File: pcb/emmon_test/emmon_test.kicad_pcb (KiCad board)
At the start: 2 copper layers, 11 parts, among them J1 Conn_01x06_Female, J2 Conn_01x08_Female, J3 Conn_01x15_Female, J4 Conn_01x15_Female, J5 Conn_01x04_Female

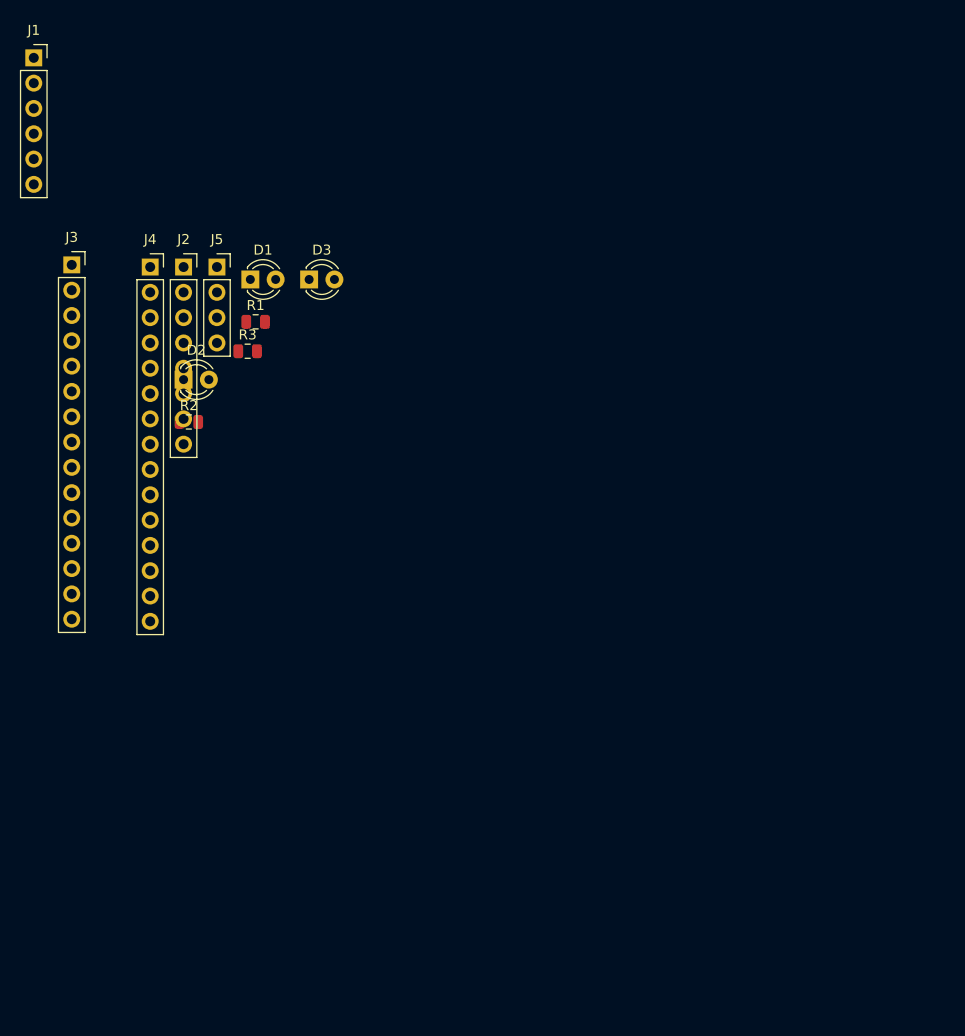
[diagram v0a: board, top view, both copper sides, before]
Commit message: se implementa oop en el codigo y se edita el pcb
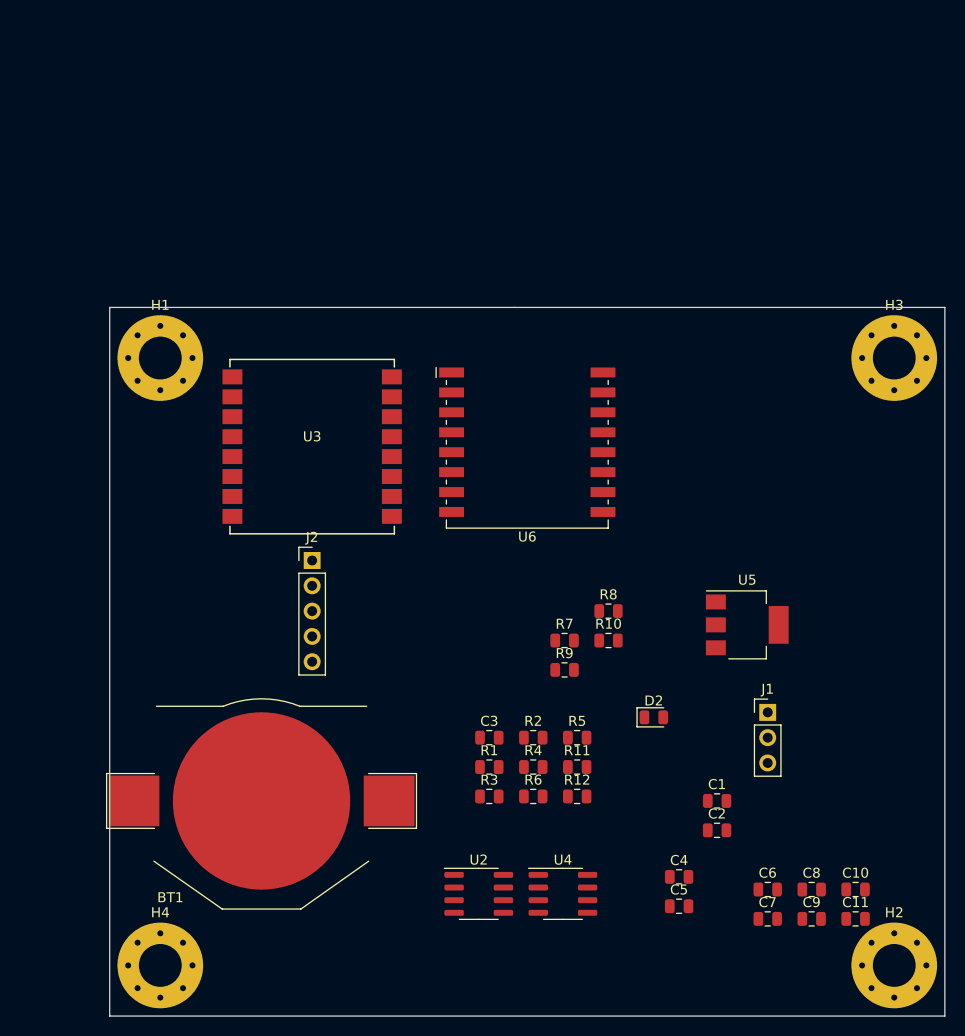
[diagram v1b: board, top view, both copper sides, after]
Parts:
- removed D1, D3: LED, LED_THT:LED_D3.0mm
- removed J3, J4: Conn_01x15_Female, Connector_PinSocket_2.54mm:PinSocket_1x15_P2.54mm_Vertical
- removed J5: Conn_01x04_Female, Connector_PinSocket_2.54mm:PinSocket_1x04_P2.54mm_Vertical
- added BT1: Battery_Cell, Battery:BatteryHolder_Keystone_3002_1x2032, F.Cu at (129.5, 105.4)
- added C1: 100n, Capacitor_SMD:C_0805_2012Metric, F.Cu at (175.3, 105.4)
- added C10: 10u, Capacitor_SMD:C_0805_2012Metric, F.Cu at (189.2, 114.3)
- added C11: 100n, Capacitor_SMD:C_0805_2012Metric, F.Cu at (189.2, 117.2)
- added C2: 47u, Capacitor_SMD:C_0805_2012Metric, F.Cu at (175.3, 108.4)
- added C3: 47p, Capacitor_SMD:C_0805_2012Metric, F.Cu at (152.4, 99.1)
- added C4: 10u, Capacitor_SMD:C_0805_2012Metric, F.Cu at (171.4, 113.0)
- added C5: 100n, Capacitor_SMD:C_0805_2012Metric, F.Cu at (171.4, 116.0)
- added C6: 10u, Capacitor_SMD:C_0805_2012Metric, F.Cu at (180.3, 114.3)
- added C7: 100n, Capacitor_SMD:C_0805_2012Metric, F.Cu at (180.3, 117.2)
- added C8: 10u, Capacitor_SMD:C_0805_2012Metric, F.Cu at (184.8, 114.3)
- added C9: 100n, Capacitor_SMD:C_0805_2012Metric, F.Cu at (184.8, 117.2)
- added H1: MountingHole_Pad, MountingHole:MountingHole_4.3mm_M4_Pad_Via, F.Cu at (119.4, 61.0)
- added H2: MountingHole_Pad, MountingHole:MountingHole_4.3mm_M4_Pad_Via, F.Cu at (193.0, 121.9)
- added H3: MountingHole_Pad, MountingHole:MountingHole_4.3mm_M4_Pad_Via, F.Cu at (193.0, 61.0)
- added H4: MountingHole_Pad, MountingHole:MountingHole_4.3mm_M4_Pad_Via, F.Cu at (119.4, 121.9)
- added R10: 12K, Resistor_SMD:R_0805_2012Metric, F.Cu at (164.4, 89.3)
- added R11: 12K, Resistor_SMD:R_0805_2012Metric, F.Cu at (161.2, 102.0)
- added R12: 12K, Resistor_SMD:R_0805_2012Metric, F.Cu at (161.2, 105.0)
- added R4: 12K, Resistor_SMD:R_0805_2012Metric, F.Cu at (156.8, 102.0)
- added R5: 12K, Resistor_SMD:R_0805_2012Metric, F.Cu at (161.2, 99.1)
- added R6: 12K, Resistor_SMD:R_0805_2012Metric, F.Cu at (156.8, 105.0)
- added R7: 12K, Resistor_SMD:R_0805_2012Metric, F.Cu at (159.9, 89.3)
- added R8: 12K, Resistor_SMD:R_0805_2012Metric, F.Cu at (164.4, 86.4)
- added R9: 12K, Resistor_SMD:R_0805_2012Metric, F.Cu at (159.9, 92.3)
- added U2: DS3231MZ, Package_SO:SOIC-8_3.9x4.9mm_P1.27mm, F.Cu at (151.3, 114.7)
- added U3: Ai-Thinker-Ra-01, RF_Module:Ai-Thinker-Ra-01-LoRa, F.Cu at (134.6, 69.8)
- added U4: AT24CS32-SSHM, Package_SO:SOIC-8_3.9x4.9mm_P1.27mm, F.Cu at (159.8, 114.7)
- added U5: AMS1117-3.3, Package_TO_SOT_SMD:SOT-223-3_TabPin2, F.Cu at (178.3, 87.7)
- added U6: ESP-07, RF_Module:ESP-07, F.Cu at (156.2, 67.3)
- D2: value LED -> LED_POWER; footprint LED_THT:LED_D3.0mm -> LED_SMD:LED_0805_2012Metric
- J1: value Conn_01x06_Female -> Conn_01x03; footprint Connector_PinSocket_2.54mm:PinSocket_1x06_P2.54mm_Vertical -> Connector_PinHeader_2.54mm:PinHeader_1x03_P2.54mm_Vertical
- J2: value Conn_01x08_Female -> Conn_01x05; footprint Connector_PinSocket_2.54mm:PinSocket_1x08_P2.54mm_Vertical -> Connector_PinHeader_2.54mm:PinHeader_1x05_P2.54mm_Vertical
- R1, R2, R3: value R_Small -> 12K
- moved J1 98.7 mm to (180.3, 96.5)
- moved D2 58.1 mm to (168.9, 97.0)
- moved R3 50.8 mm to (152.4, 105.0)
- moved R1 50.5 mm to (152.4, 102.0)
- moved R2 46.9 mm to (156.8, 99.1)
- moved J2 32.2 mm to (134.6, 81.3)
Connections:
- D2 pad 1: Net-(D2-Pad1) -> GND
- J1 pad 1: Net-(J1-Pad1) -> +3V3
- J1 pad 2: Net-(J1-Pad2) -> PULSES
- J1 pad 3: Net-(J1-Pad3) -> GND
- J2 pad 1: Net-(J2-Pad1) -> +3V3
- J2 pad 2: Net-(J2-Pad2) -> TX
- J2 pad 3: Net-(J2-Pad3) -> ALARM
- J2 pad 4: Net-(J2-Pad4) -> PULSES
- J2 pad 5: Net-(J2-Pad5) -> GND
- R1 pad 1: Net-(R1-Pad1) -> DIO0
- R1 pad 2: Net-(R1-Pad2) -> +3V3
- R2 pad 1: Net-(R2-Pad1) -> ALARM
- R2 pad 2: Net-(R2-Pad2) -> +3V3
- R3 pad 1: Net-(R3-Pad1) -> PULSES
- R3 pad 2: Net-(R3-Pad2) -> +3V3
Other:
- board outline added: 83.8 x 71.1 mm
